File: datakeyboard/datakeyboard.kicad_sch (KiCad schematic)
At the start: 41 parts, among them Q1 BSS83P, Q2 BSS83P, Q3 BSS83P, SW1 SW_Push, SW2 SW_Push, SW3 SW_Push, SW4 SW_Push, SW5 SW_Push, SW6 SW_Push, U1 PIC24FJ128GB204, U2 TP4056, U3 MIC5501-30

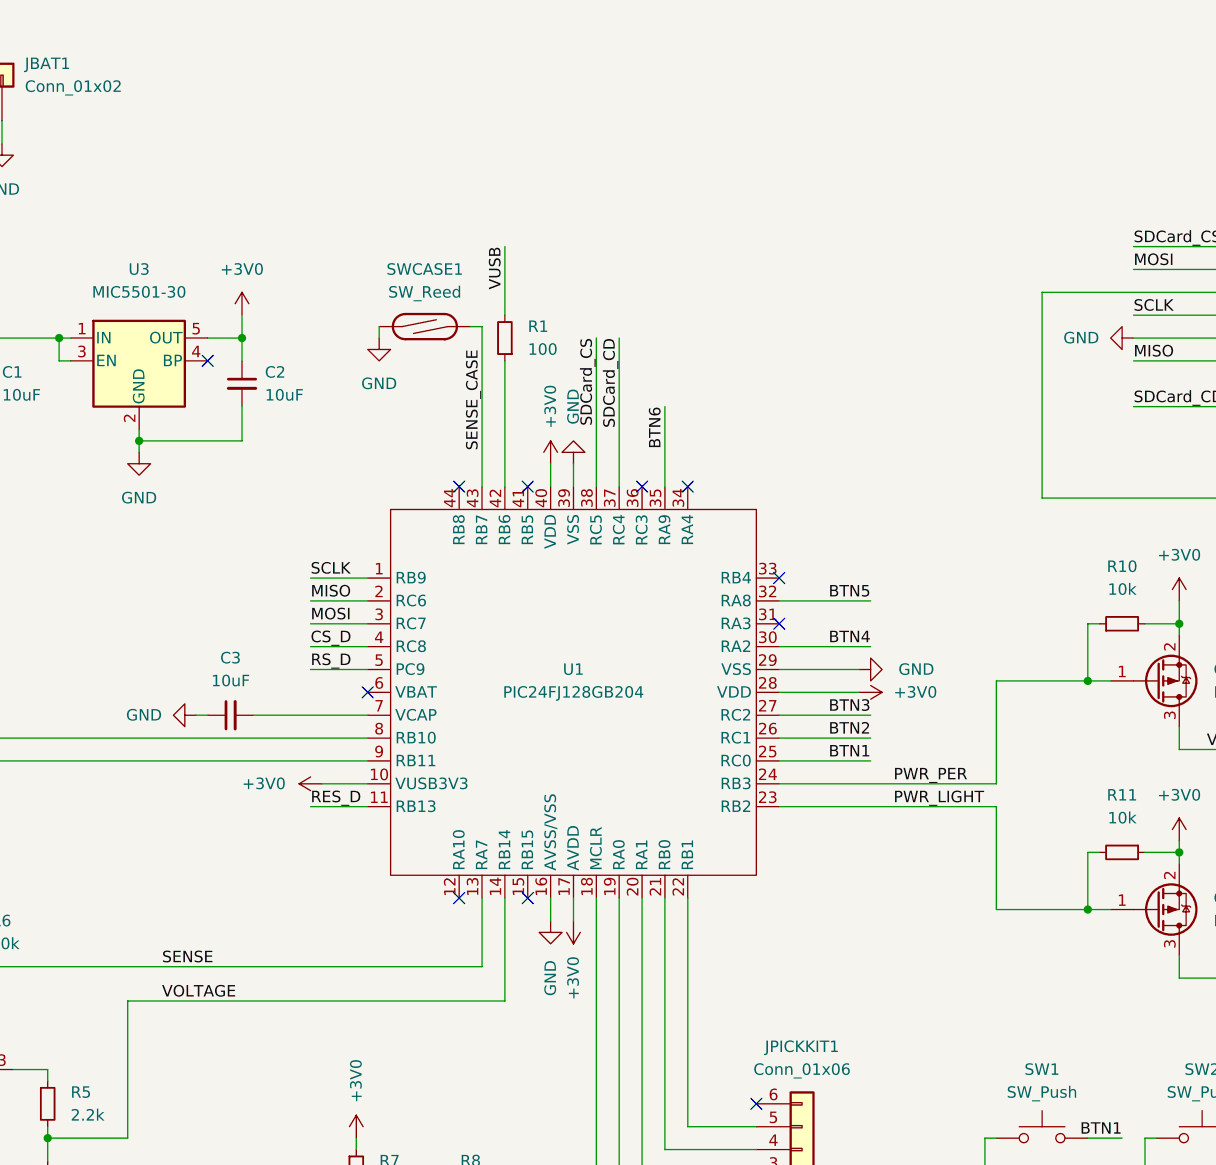
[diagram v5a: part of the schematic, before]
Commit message: Fine tune schematic (grounding pins)
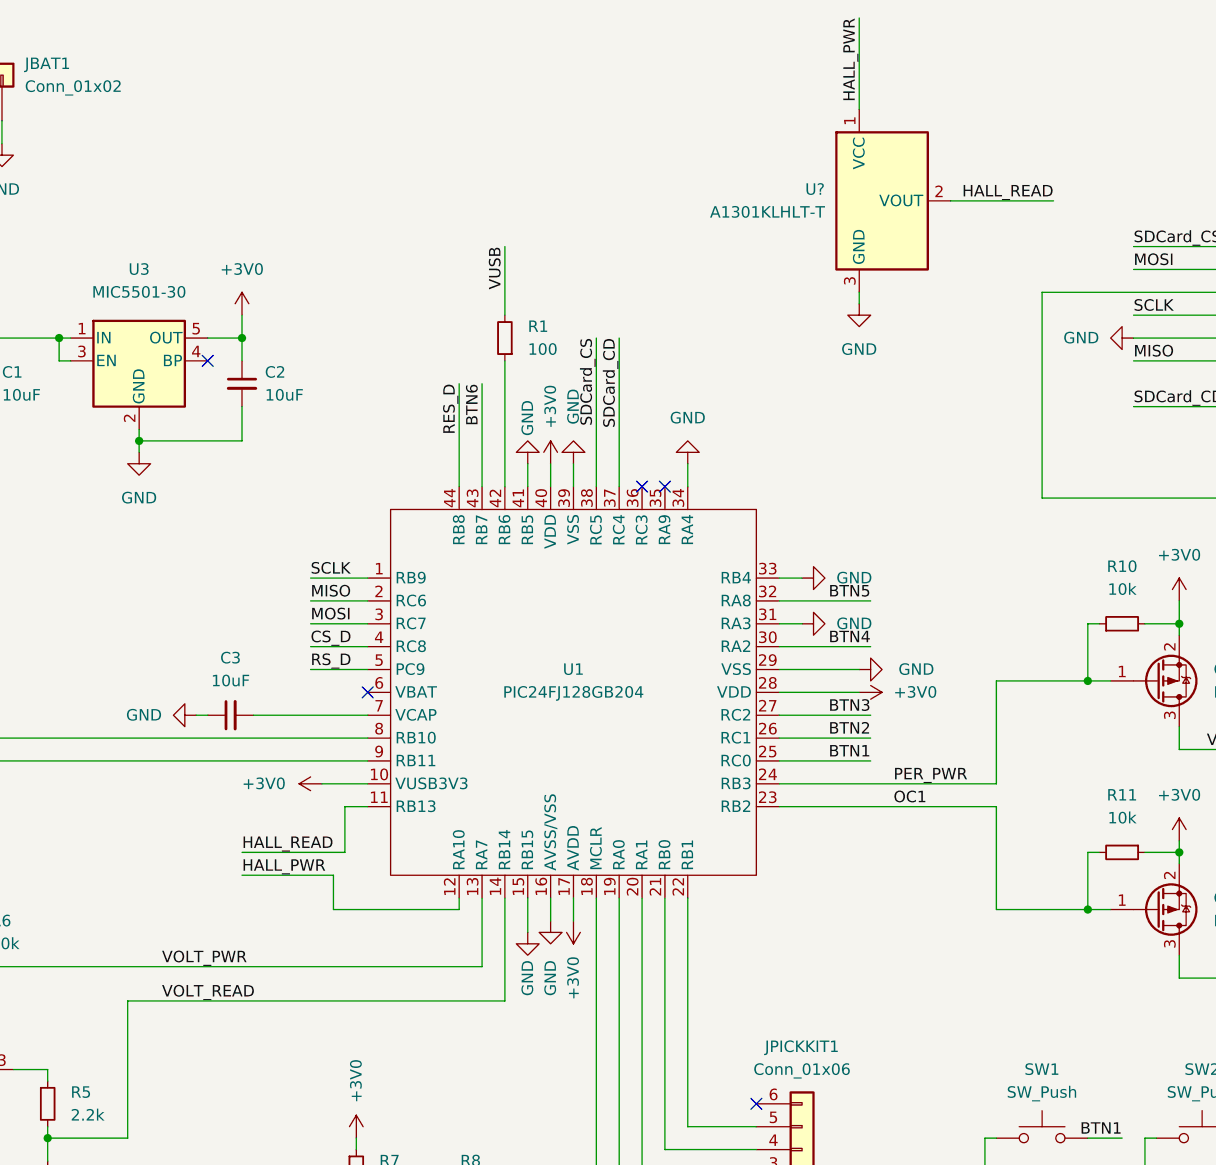
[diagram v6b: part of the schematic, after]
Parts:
- removed SWCASE1: SW_Reed, symbol Switch:SW_Reed
- added U?: A1301KLHLT-T, Package_TO_SOT_SMD:SOT-23W, symbol Sensor_Magnetic:A1301KLHLT-T
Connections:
- net SENSE_CASE is gone; now on net BTN6: U1.43 (RB7)
- net BTN6: no longer U1.35 (RA9)
- net GND: now also U1.15 (RB15), U1.31 (RA3), U1.33 (RB4), U1.34 (RA4), U1.41 (RB5), U?.3 (GND)
- net RES_D: now also U1.44 (RB8); no longer U1.11 (RB13)
- net HALL_PWR: now reaches U1.12 (RA10)
- net HALL_PWR: now also U?.1 (VCC)
- net PWR_LIGHT renamed OC1
- net PWR_PER renamed PER_PWR
- net SENSE renamed VOLT_PWR
- net VOLTAGE renamed VOLT_READ
- new net HALL_READ: U1.11 (RB13), U?.2 (VOUT)
- no-connect marks 15 -> 9

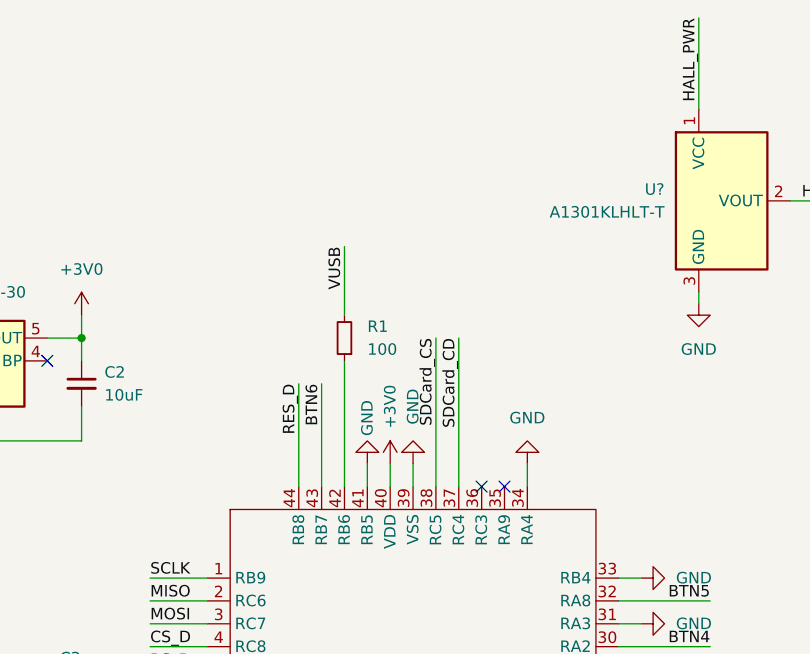
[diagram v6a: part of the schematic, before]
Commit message: Add case switch
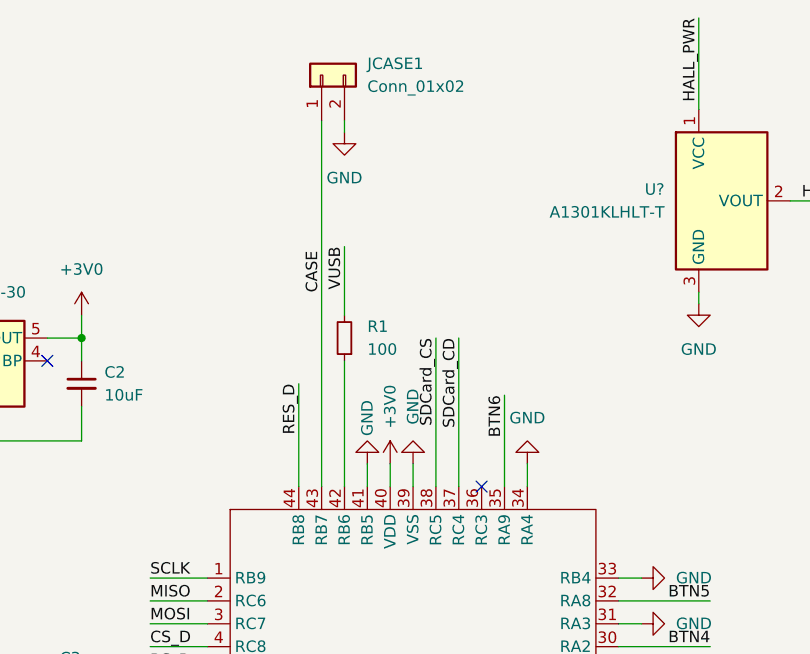
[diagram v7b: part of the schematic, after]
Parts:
- added JCASE1: Conn_01x02, symbol Connector_Generic:Conn_01x02
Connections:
- net BTN6: now also U1.35 (RA9); no longer U1.43 (RB7)
- net GND: now also JCASE1.2 (Pin_2)
- new net CASE: JCASE1.1 (Pin_1), U1.43 (RB7)
- no-connect marks 9 -> 8
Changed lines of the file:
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@@
   (no_connect (at 227.33 38.1))
   (no_connect (at 55.88 100.33))
-  (no_connect (at 165.1 67.31))
   (no_connect (at 132.08 90.17))
   (no_connect (at 175.26 135.89))
@@
     (stroke (width 0) (type default) (color 0 0 0 0))
   )
+  (wire (pts (xy 165.1 57.15) (xy 165.1 67.31))
+    (stroke (width 0) (type default) (color 0 0 0 0))
+  )
   (wire (pts (xy 81.28 113.03) (xy 81.28 132.08))
     (stroke (width 0) (type default) (color 0 0 0 0))
@@
     (stroke (width 0) (type default) (color 0 0 0 0))
   )
-  (wire (pts (xy 144.78 55.88) (xy 144.78 67.31))
+  (wire (pts (xy 144.78 26.67) (xy 144.78 67.31))
     (stroke (width 0) (type default) (color 0 0 0 0))
   )
@@
   )
   (wire (pts (xy 96.52 138.43) (xy 96.52 139.7))
+    (stroke (width 0) (type default) (color 0 0 0 0))
+  )
+  (wire (pts (xy 147.32 26.67) (xy 147.32 27.94))
     (stroke (width 0) (type default) (color 0 0 0 0))
   )
@@
     (effects (font (size 1.27 1.27)) (justify left bottom))
   )
+  (label "CASE" (at 144.78 45.72 90)
+    (effects (font (size 1.27 1.27)) (justify left bottom))
+  )
   (label "PER_PWR" (at 190.5 100.33 0)
     (effects (font (size 1.27 1.27)) (justify left bottom))
@@
     (effects (font (size 1.27 1.27)) (justify right bottom))
   )
-  (label "BTN6" (at 144.78 55.88 270)
+  (label "BTN6" (at 165.1 57.15 270)
     (effects (font (size 1.27 1.27)) (justify right bottom))
   )
@@
     (pin "1")
   )
+  (symbol (lib_id "power:GND") (at 147.32 27.94 0) (unit 1)
+    (in_bom yes) (on_board yes) (fields_autoplaced)
+    (property "Reference" "#PWR?" (id 0) (at 147.32 34.29 0)
+      (effects (font (size 1.27 1.27)) hide)
+    )
+    (property "Value" "GND" (id 1) (at 147.32 33.02 0))
+    (property "Footprint" "" (id 2) (at 147.32 27.94 0)
+      (effects (font (size 1.27 1.27)) hide)
+    )
+    (property "Datasheet" "" (id 3) (at 147.32 27.94 0)
+      (effects (font (size 1.27 1.27)) hide)
+    )
+    (pin "1")
+  )
   (symbol (lib_id "power:GND") (at 218.44 157.48 0) (unit 1)
     (in_bom yes) (on_board yes) (fields_autoplaced)
@@
     )
     (property "Datasheet" "~" (id 3) (at 39.37 176.53 0)
+      (effects (font (size 1.27 1.27)) hide)
+    )
+    (pin "1")
+    (pin "2")
+  )
+  (symbol (lib_id "Connector_Generic:Conn_01x02") (at 144.78 21.59 90) (unit 1)
+    (in_bom yes) (on_board yes) (fields_autoplaced)
+    (property "Reference" "JCASE1" (id 0) (at 149.86 20.3199 90)
+      (effects (font (size 1.27 1.27)) (justify right))
+    )
+    (property "Value" "Conn_01x02" (id 1) (at 149.86 22.8599 90)
+      (effects (font (size 1.27 1.27)) (justify right))
+    )
+    (property "Footprint" "" (id 2) (at 144.78 21.59 0)
+      (effects (font (size 1.27 1.27)) hide)
+    )
+    (property "Datasheet" "~" (id 3) (at 144.78 21.59 0)
       (effects (font (size 1.27 1.27)) hide)
     )
@@
       (reference "#PWR?") (unit 1) (value "GND") (footprint "")
     )
+    (path "/8984821a-d82e-42e3-a101-90c33ff8813c"
+      (reference "#PWR?") (unit 1) (value "GND") (footprint "")
+    )
     (path "/cb39e6f7-76ef-4ce7-88db-0cf1edbda03c"
       (reference "#PWR?") (unit 1) (value "GND") (footprint "")
@@
       (reference "JCARD1") (unit 1) (value "Micro_SD_Card_Det") (footprint "")
     )
+    (path "/a0d77163-a822-4f35-a314-d39c42d23672"
+      (reference "JCASE1") (unit 1) (value "Conn_01x02") (footprint "")
+    )
     (path "/d37334a6-f13d-49cb-afe8-430745ecfc0f"

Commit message: Board layout
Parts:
- removed U?: A1301KLHLT-T, Package_TO_SOT_SMD:SOT-23W, symbol Sensor_Magnetic:A1301KLHLT-T
- added C6: 100nF, Capacitor_SMD:C_0603_1608Metric_Pad1.08x0.95mm_HandSolder, symbol Device:C_Small
- C1, C2, C3: footprint (none) -> Capacitor_SMD:C_0805_2012Metric_Pad1.18x1.45mm_HandSolder
- C10: renamed from C9; footprint (none) -> Capacitor_SMD:C_0603_1608Metric_Pad1.08x0.95mm_HandSolder
- C11: renamed from C10; footprint (none) -> Capacitor_SMD:C_0603_1608Metric_Pad1.08x0.95mm_HandSolder
- C4: renamed from C5; footprint (none) -> Capacitor_SMD:C_0603_1608Metric_Pad1.08x0.95mm_HandSolder
- C5: renamed from C4; footprint (none) -> Capacitor_SMD:C_0603_1608Metric_Pad1.08x0.95mm_HandSolder
- C7: renamed from C6; footprint (none) -> Capacitor_SMD:C_0603_1608Metric_Pad1.08x0.95mm_HandSolder
- C8: renamed from C7; footprint (none) -> Capacitor_SMD:C_0603_1608Metric_Pad1.08x0.95mm_HandSolder
- C9: renamed from C8; footprint (none) -> Capacitor_SMD:C_0603_1608Metric_Pad1.08x0.95mm_HandSolder
- D1, D2: footprint (none) -> LED_SMD:LED_0805_2012Metric_Pad1.15x1.40mm_HandSolder
- JBAT1, JCASE1: footprint (none) -> Connector_PinHeader_2.54mm:PinHeader_1x02_P2.54mm_Vertical
- JCARD1: footprint (none) -> Connector_Card:microSD_HC_Hirose_DM3AT-SF-PEJM5
- JDISP1: footprint (none) -> Connector_PinHeader_2.54mm:PinHeader_1x08_P2.54mm_Vertical
- JPICKKIT1: footprint (none) -> Connector_PinHeader_2.54mm:PinHeader_1x06_P2.54mm_Vertical
- JUSB1: footprint (none) -> Connector_USB:USB_Micro-B_Molex-105017-0001
- R1, R10, R11, R2, R3, R4, R5, R6, R7, R8, R9: footprint (none) -> Resistor_SMD:R_0805_2012Metric_Pad1.20x1.40mm_HandSolder
- SW1, SW2, SW3, SW4, SW5, SW6: footprint (none) -> Button_Switch_SMD:SW_Push_1P1T_NO_6x6mm_H9.5mm
- U1: footprint (none) -> Package_QFP:TQFP-44_10x10mm_P0.8mm
- U2: footprint (none) -> Package_SO:SO-8_5.3x6.2mm_P1.27mm
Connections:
- net +3V0: now also C6.1
- net GND: now also C6.2
- net HALL_PWR: no longer names the net of U1.12 (RA10)
- net HALL_READ: no longer names the net of U1.11 (RB13)
- no-connect marks 8 -> 10
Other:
- moved on the sheet: C10, C7, C8, C9
